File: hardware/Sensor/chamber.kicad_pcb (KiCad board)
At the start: 2 copper layers, 100 x 100 mm, 57 parts, among them J10 RF_Shield_Two_Pieces, J11 Conn_Coaxial, J20 RF_Shield_Two_Pieces, Q20 BC859, Q21 Q_NMOS_GDS, U1 L7805, U10 LMC662, U11 LM358, U20 MC34063AD, U30 STM32F070F6Px, U31 MCP3425A0T-ECH

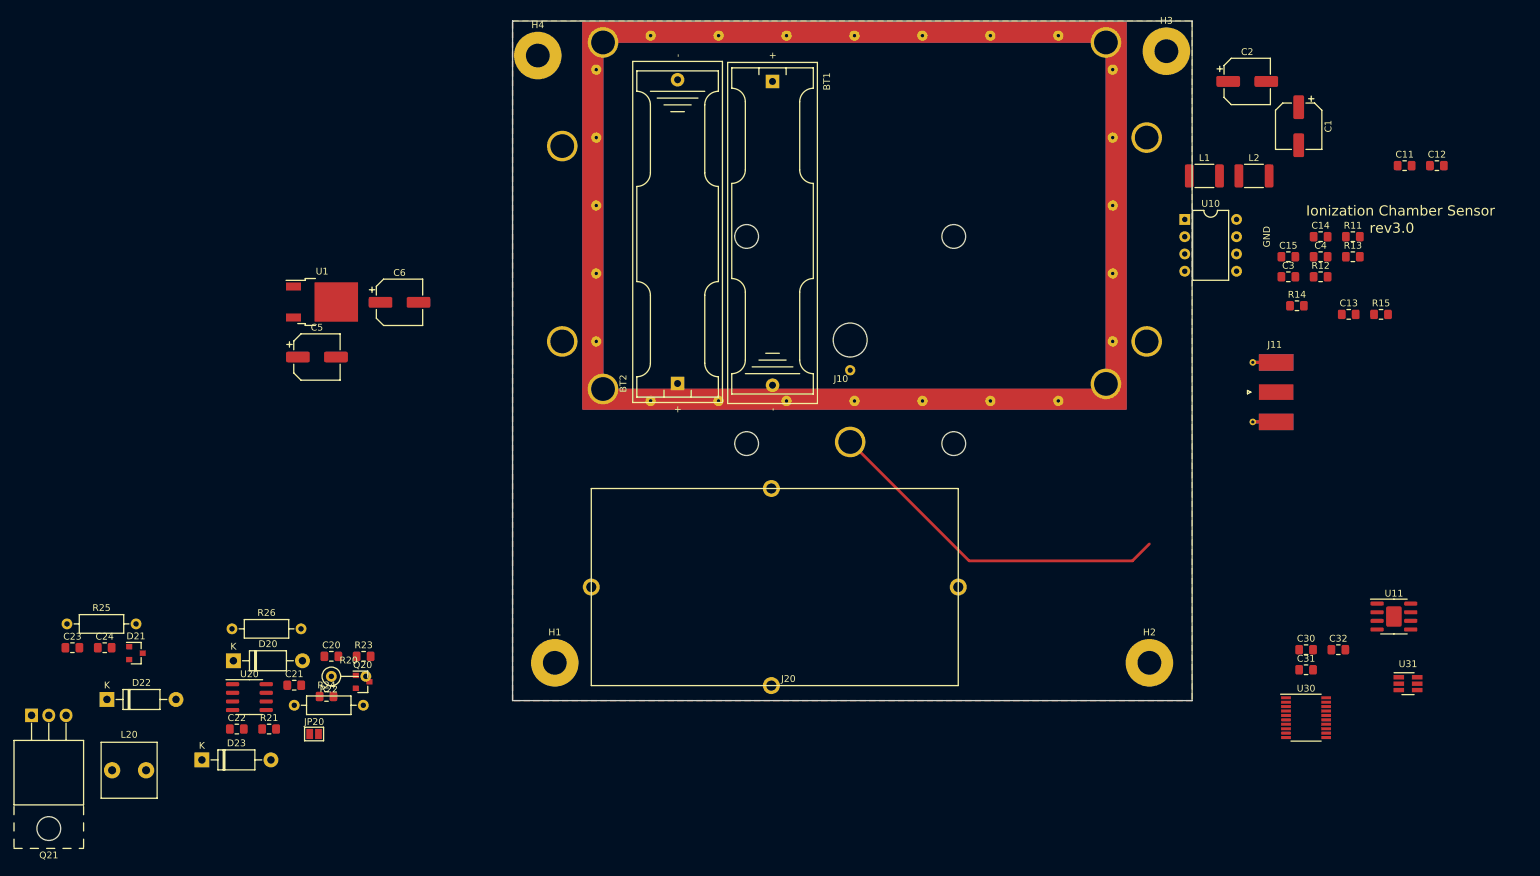
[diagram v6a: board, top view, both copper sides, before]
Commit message: draft of element placement
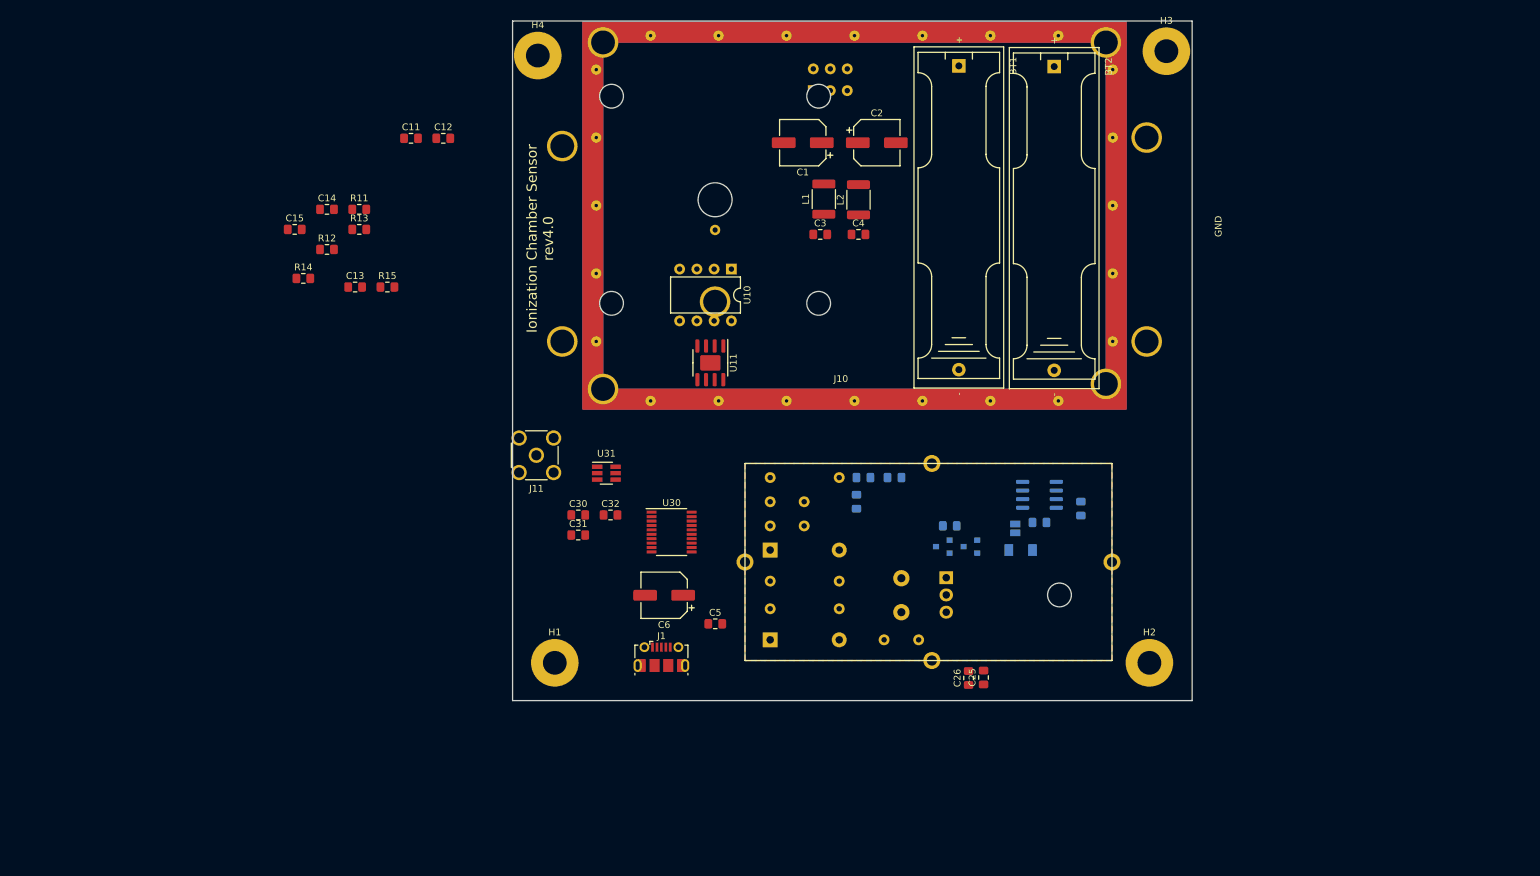
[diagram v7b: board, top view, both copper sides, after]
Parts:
- removed U1: L7805, Package_TO_SOT_SMD:TO-252-2
- added C25: 100n, Capacitor_SMD:C_0805_2012Metric_Pad1.15x1.40mm_HandSolder, F.Cu at (69.3, 96.6)
- added C26: 100n, Capacitor_SMD:C_0805_2012Metric_Pad1.15x1.40mm_HandSolder, F.Cu at (67.1, 96.7)
- added J1: USB_B_Micro, Connector_USB:USB_Micro-B_Molex-105017-0001, F.Cu at (21.9, 93.6)
- added SW1: SW_DPDT_x2, Button_Switch_THT:SW_E-Switch_EG1271_DPDT, B.Cu at (44.3, 10.2)
- C20, C21, C22, D20, D21, D22, J20, JP20, L20, Q20, Q21, R20, R21, R22, R23, R24, R25, R26, U20: moved to B.Cu
- C23, C24: footprint Capacitor_SMD:C_0805_2012Metric_Pad1.15x1.40mm_HandSolder -> Capacitor_THT:C_Disc_D8.0mm_W2.5mm_P5.00mm; moved to B.Cu
- C5: value 100u/16V -> 100n; footprint Capacitor_SMD:CP_Elec_6.3x5.4 -> Capacitor_SMD:C_0805_2012Metric_Pad1.15x1.40mm_HandSolder
- C6: value 100u/16V -> 10u/16V
- D23: footprint Diode_THT:D_DO-41_SOD81_P10.16mm_Horizontal -> Diode_SMD:D_MiniMELF; moved to B.Cu
- J11: footprint Connector_Coaxial:SMA_Molex_73251-1153_EdgeMount_Horizontal -> Connector_Coaxial:SMA_Molex_73251-2200_Horizontal
- moved C11 146.3 mm to (-14.9, 17.3)
- moved C12 146.3 mm to (-10.2, 17.3)
- moved C13 146.3 mm to (-23.2, 39.1)
- moved C14 146.3 mm to (-27.3, 27.7)
- moved C15 146.3 mm to (-32.1, 30.7)
- moved R11 146.3 mm to (-22.6, 27.7)
- moved R12 146.3 mm to (-27.3, 33.6)
- moved R13 146.3 mm to (-22.6, 30.7)
- moved R14 146.3 mm to (-30.8, 37.9)
- moved R15 146.3 mm to (-18.4, 39.1)
- moved Q21 136.1 mm to (63.8, 81.9), turned to 270 degrees
- moved D23 124.4 mm to (74.8, 77.8)
- moved U31 122.0 mm to (13.8, 66.5)
- moved U20 120.0 mm to (77.5, 69.7), turned to 180 degrees
- moved D21 119.8 mm to (63.3, 77.3), turned to 180 degrees
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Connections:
- BT1 pad 1: (no net) -> Net-(BT1-Pad1)
- BT2 pad 1: (no net) -> Net-(BT2-Pad1)
- C5 pad 1: +BATT -> GND
- C5 pad 2: GND -> +5V
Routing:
- net Net-(D22-Pad1): track 52.3 -> 0.00 mm
- added copper zone on B.Cu, net (none)
- removed copper zone on B.Cu, net GND
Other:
- board text added: "Ionization Chamber Sensor rev4.0"
- board text removed: "Ionization Chamber Sensor"
- board text removed: "rev3.0"

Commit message: grouped elements and grounds
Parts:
- removed C25, C26, C5: 100n, Capacitor_SMD:C_0805_2012Metric_Pad1.15x1.40mm_HandSolder
- removed D20: 1N4007, Diode_THT:D_DO-41_SOD81_P10.16mm_Horizontal
- removed J10: RF_Shield_Two_Pieces, IonizationChamber:IonizationChamberShield
- added C35: 100n, Capacitor_SMD:C_0805_2012Metric_Pad1.15x1.40mm_HandSolder, B.Cu at (62.0, 91.9)
- added C42: 100n, Capacitor_SMD:C_0805_2012Metric_Pad1.15x1.40mm_HandSolder, F.Cu at (31.3, 92.4)
- added C51: 10n, Capacitor_Tantalum_SMD:CP_EIA-3528-21_Kemet-B, F.Cu at (-22.3, 72.2)
- added C54: 100n, Capacitor_SMD:C_0805_2012Metric_Pad1.15x1.40mm_HandSolder, F.Cu at (-3.95, 69.6)
- added C55: 100n, Capacitor_SMD:C_0805_2012Metric_Pad1.15x1.40mm_HandSolder, F.Cu at (-10.9, 77.8)
- added C56: 10n, Capacitor_Tantalum_SMD:CP_EIA-3528-21_Kemet-B, F.Cu at (-11.7, 72.2)
- added C57: 100n, Capacitor_SMD:C_0805_2012Metric_Pad1.15x1.40mm_HandSolder, F.Cu at (-17.0, 66.0)
- added D33: 1N4007, Diode_THT:D_DO-41_SOD81_P10.16mm_Horizontal, B.Cu at (53.3, 90.3)
- added J33: RF_Shield_Two_Pieces, IonizationChamber:IonizationChamberShield, F.Cu at (10.3, 57.1)
- added R50: 0R, Resistor_SMD:R_0805_2012Metric_Pad1.15x1.40mm_HandSolder, F.Cu at (-3.95, 72.5)
- added R51: 0R, Resistor_SMD:R_0805_2012Metric_Pad1.15x1.40mm_HandSolder, F.Cu at (-10.9, 80.7)
- added R52: 22k, Resistor_SMD:R_0805_2012Metric_Pad1.15x1.40mm_HandSolder, F.Cu at (-6.20, 77.8)
- added R53: R, Resistor_SMD:R_0805_2012Metric_Pad1.15x1.40mm_HandSolder, F.Cu at (-6.20, 80.7)
- added R55: R, Resistor_SMD:R_0805_2012Metric_Pad1.15x1.40mm_HandSolder, F.Cu at (-27.9, 66.8)
- added TP30: TestPoint, TestPoint:TestPoint_Loop_D2.60mm_Drill0.9mm_Beaded, B.Cu at (59.1, 68.9)
- added U51: Opamp_Dual_Generic, Package_SO:SOIC-8_3.9x4.9mm_P1.27mm, F.Cu at (-23.4, 79.5)
- added U52: MCP3425A0T-ECH, Package_TO_SOT_SMD:SOT-23-6_Handsoldering, F.Cu at (-16.2, 78.6)
- C44: renamed from C6; footprint Capacitor_SMD:CP_Elec_6.3x5.4 -> Capacitor_Tantalum_SMD:CP_EIA-3528-21_Kemet-B; moved to B.Cu
- D34: renamed from D22; moved to F.Cu
- H31: renamed from H1; footprint MountingHole:MountingHole_3.5mm_Pad -> MountingHole:MountingHole_3.5mm
- H32: renamed from H2; footprint MountingHole:MountingHole_3.5mm_Pad -> MountingHole:MountingHole_3.5mm
- H33: renamed from H3; footprint MountingHole:MountingHole_3.5mm_Pad -> MountingHole:MountingHole_3.5mm
- H34: renamed from H4; footprint MountingHole:MountingHole_3.5mm_Pad -> MountingHole:MountingHole_3.5mm
- Q32: renamed from Q21; footprint Package_TO_SOT_THT:TO-220-3_Horizontal_TabUp -> Package_TO_SOT_THT:TO-220-3_Horizontal_TabDown
- U33: renamed from U11; footprint Package_SO:SOIC-8-1EP_3.9x4.9mm_P1.27mm_EP2.29x3mm -> Package_SO:SOIC-8_3.9x4.9mm_P1.27mm
- moved C45 69.7 mm to (34.5, 51.3), turned to 270 degrees
- moved R41 62.0 mm to (31.0, 43.2), turned to 90 degrees
- moved C48 57.3 mm to (34.0, 42.2), turned to 180 degrees
- moved R39 55.9 mm to (28.4, 38.1)
- moved C40 55.8 mm to (28.4, 30.0)
- moved R38 54.3 mm to (31.5, 22.9), turned to 180 degrees
- moved R42 52.7 mm to (34.0, 44.2), turned to 180 degrees
- moved R40 51.3 mm to (28.5, 35.6), turned to 180 degrees
- moved C47 48.0 mm to (33.0, 38.1)
- moved C46 46.6 mm to (31.5, 20.3), turned to 180 degrees
- moved D34 44.9 mm to (53.5, 48.9), turned to 90 degrees
- moved C44 39.3 mm to (61.5, 87.9), turned to 90 degrees
- moved R37 23.6 mm to (53.8, 69.1), turned to 180 degrees
- moved C41 21.9 mm to (47.8, 90.3), turned to 180 degrees
- moved R33 18.9 mm to (48.2, 83.0), turned to 90 degrees
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- renumbered BT1 to BT31, BT2 to BT32, C21 to C31, C20 to C32, C1 to C33, C2 to C34, C3 to C37, C4 to C38, C22 to C39, C14 to C40, C23 to C41, C24 to C43, C15 to C45, C11 to C46, C12 to C47, C13 to C48, C32 to C50, C30 to C52, C31 to C53, D23 to D31, D21 to D32, J1 to J31, J20 to J32, J11 to J34, JP20 to JP31, L20 to L31, L1 to L32, L2 to L33, Q20 to Q31, R20 to R31, R21 to R32, R22 to R33, R23 to R34, R24 to R35, R25 to R36, R26 to R37, R11 to R38, R12 to R39, R13 to R40, R14 to R41, R15 to R42, SW1 to SW31, U31 to U1, U20 to U31, U10 to U32, U30 to U36, V10 to V31
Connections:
- C48 pad 1: Net-(C13-Pad1) -> Net-(C48-Pad1)
- C48 pad 2: GND -> Net-(C48-Pad2)
- R40 pad 1: Net-(R13-Pad1) -> Net-(C48-Pad1)
- R41 pad 2: Net-(C13-Pad1) -> Net-(C48-Pad2)
- U32 pad 7: Net-(R13-Pad1) -> Net-(C48-Pad1)
- U33 pad 3: Net-(R13-Pad1) -> GND
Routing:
- net GND: track 0.00 -> 96.4 mm
- net +5V: track 0.00 -> 10.5 mm
- added copper zone on B.Cu, net GND
- removed copper zone on B.Cu, net (none)
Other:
- board text removed: "GND"
